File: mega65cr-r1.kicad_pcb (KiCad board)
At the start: 4 copper layers, 435 x 140.6 mm, 185 parts, among them J1 DB9_Male_MountingHoles, J10 Molex 46765-2301, J11 CON-SOCJ-2155, J12 Header for power lead to QMTE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, J13 Conn_01x04_Male, J14 Conn_02x17_Odd_Even, J15 696101000002 Fuse Holder 20mm, J16 Conn_01x04_Male, J17 C64_Tape_Port, J18 BA60BC0WT, J19 C64_User_Port, J2 DB9_Male_MountingHoles, J20 C64_Expansion_Port, J21 Audio Header, J22 DB15_Female_HighDensity_Mount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, J23 3.5mm_Stereo_Audio_Jack STX-3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, J24 Component A/V, J25 Joystick Ports Mezannine Lower, J26 Joystick Ports Mezannine Upper, J3 Wuerth_7499010121A, J4 QMTECH FPGA Module U4, J5 QMTECH FPGA Module U5, J6 SDF-60J for IEC 1541 serial p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, J7 QMTECH JTAG, J8 RTC, J9 1140084168 microSD Card Slot, P1 Full-side CD Card Slot, SW1 SW_Push_DPDT, SW2 SW_SPDT_with_shield, U1 74LS373, U10 74LS06N, U11 74LS06N, U12 DP83826, U13 74LVC374, U14 PTN3363BSMP, U15 LM2678T-5.0, U16 74LVC374, U17 74LVC374, U18 74LS374, U19 74LS374, U2 74LVC374, U20 74LS125, U21 74LS125, U22 74LS06N, U23 74LVC374, U24 74LS125, U25 74LS374, U26 74LS374, U27 74LS138, U28 74LS138, U29 74LS137, U3 74LVC374, U30 74LS137, U31 74LS04, U32 74LVC374, U33 74LVC374, U34 74LVC374, U35 74LS374, U36 74LS374, U37 74LS374, U38 74LVC374, U39 74LVC374, U4 74LS373, U40 74LS374, U41 74LS374, U5 74LS06N, U6 74LVC374, U7 74LVC374, U8 74LS374, U9 74LS373

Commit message: place some mounting holes and reset button #3
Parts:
- added H1: MountingHole_Pad, MountingHole:MountingHole_3.2mm_M3_DIN965_Pad, F.Cu at (35.0, 55.0)
- added H2: MountingHole_Pad, MountingHole:MountingHole_3.2mm_M3_DIN965_Pad, F.Cu at (62.0, 144.0)
- added H3: MountingHole_Pad, MountingHole:MountingHole_3.2mm_M3_DIN965_Pad, F.Cu at (331.8, 85.6)
- added H4: MountingHole_Pad, MountingHole:MountingHole_3.2mm_M3_DIN965_Pad, F.Cu at (338.9, 85.6)
- added H5: MountingHole_Pad, MountingHole:MountingHole_3.2mm_M3_DIN965_Pad, F.Cu at (331.8, 92.8)
- added H6: MountingHole_Pad, MountingHole:MountingHole_3.2mm_M3_DIN965_Pad, F.Cu at (324.6, 99.9)
- added H7: MountingHole_Pad, MountingHole:MountingHole_3.2mm_M3_DIN965_Pad, F.Cu at (324.6, 92.8)
- added H8: MountingHole_Pad, MountingHole:MountingHole_3.2mm_M3_DIN965_Pad, F.Cu at (317.5, 85.6)
- added H9: MountingHole_Pad, MountingHole:MountingHole_3.2mm_M3_DIN965_Pad, F.Cu at (317.5, 99.9)
- added J27: USB Blaster JTAG, Connector_PinHeader_2.54mm:PinHeader_2x05_P2.54mm_Vertical, F.Cu at (323.4, 113.4)
- added J28: UART, Connector_PinHeader_2.54mm:PinHeader_1x03_P2.54mm_Vertical, F.Cu at (316.2, 128.2)
- added J30: Keyboard JTAG header, Connector_PinHeader_2.54mm:PinHeader_2x05_P2.54mm_Vertical, F.Cu at (316.2, 113.4)
- added JP1: KBD JTAG EN, Connector_PinHeader_2.54mm:PinHeader_1x03_P2.54mm_Vertical, F.Cu at (330.6, 113.4)
- added U43: 74LVC374, Package_DIP:DIP-20_W7.62mm, F.Cu at (273.8, 84.1)
- added U44: 74LS374, Package_DIP:DIP-20_W7.62mm, F.Cu at (284.7, 84.1)
- J23: value 3.5mm_Stereo_Audio_Jack STX-3500-4N -> Audio Out
- JB1: value TE0790-03 -> TE0790-03 JTAG + UART
- SW1: value SW_Push_DPDT -> Reset Button
- moved SW1 43.5 mm to (48.0, 144.0), turned to 90 degrees
- moved J25 17.5 mm to (109.1, 135.1)
- moved J2 14.3 mm to (40.9, 115.5)
- moved J1 12.5 mm to (41.0, 84.0)
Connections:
- net /Cartridge Port/NMI_N renamed NMI_N
- net /FPGA Module/BANK12_N26 renamed KB_IO3
- net /FPGA Module/BANK12_P23 renamed KB_IO2
- net /FPGA Module/BANK12_R25 renamed KB_IO1
- net /Power Supply/VBAT renamed /Power Supply & Mounting Holes/VBAT
- net /VGA & Component AV/COMP_CHROMA renamed /VGA, C64 AV & C64 Keyboard/COMP_CHROMA
- net /VGA & Component AV/COMP_LUMA renamed /VGA, C64 AV & C64 Keyboard/COMP_LUMA
- net /VGA & Component AV/VGA_B renamed /VGA, C64 AV & C64 Keyboard/VGA_B
- net /VGA & Component AV/VGA_G renamed /VGA, C64 AV & C64 Keyboard/VGA_G
- net /VGA & Component AV/VGA_R renamed /VGA, C64 AV & C64 Keyboard/VGA_R
- net /VGA & Component AV/VGA_SCL renamed /VGA, C64 AV & C64 Keyboard/VGA_SCL
- net /VGA & Component AV/VGA_SDA renamed /VGA, C64 AV & C64 Keyboard/VGA_SDA
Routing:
- net /Power Supply & Mounting Holes/VBAT: track 74.1 -> 76.7 mm

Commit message: add and position mounting holes #3
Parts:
- added H10: MountingHole_Pad, MountingHole:MountingHole_3.2mm_M3_DIN965_Pad, F.Cu at (257.0, 50.0)
- added H11: MountingHole_Pad, MountingHole:MountingHole_3.2mm_M3_DIN965_Pad, F.Cu at (317.0, 50.0)
- added H12: MountingHole_Pad, MountingHole:MountingHole_3.2mm_M3_DIN965_Pad, F.Cu at (335.0, 40.0)
- added H13: MountingHole_Pad, MountingHole:MountingHole_3.2mm_M3_DIN965_Pad, F.Cu at (365.0, 40.0)
- added H14: MountingHole_Pad, MountingHole:MountingHole_3.2mm_M3_DIN965_Pad, F.Cu at (375.0, 40.0)
- added H15: MountingHole_Pad, MountingHole:MountingHole_3.2mm_M3_DIN965_Pad, F.Cu at (405.0, 40.0)
- added H16: MountingHole_Pad, MountingHole:MountingHole_3.2mm_M3_DIN965_Pad, F.Cu at (257.0, 110.0)
- added H17: MountingHole_Pad, MountingHole:MountingHole_3.2mm_M3_DIN965_Pad, F.Cu at (317.0, 110.0)
- moved H5 211.6 mm to (122.0, 64.9)
- moved H6 207.4 mm to (122.0, 144.0)
- moved H3 197.2 mm to (137.0, 55.0)
- moved H9 151.0 mm to (460.0, 50.0)
- moved H8 108.5 mm to (420.0, 50.0)
- moved H4 105.0 mm to (238.5, 55.0)
- moved H7 100.2 mm to (238.5, 144.0)
- moved J24 2.17 mm to (349.8, 37.9)

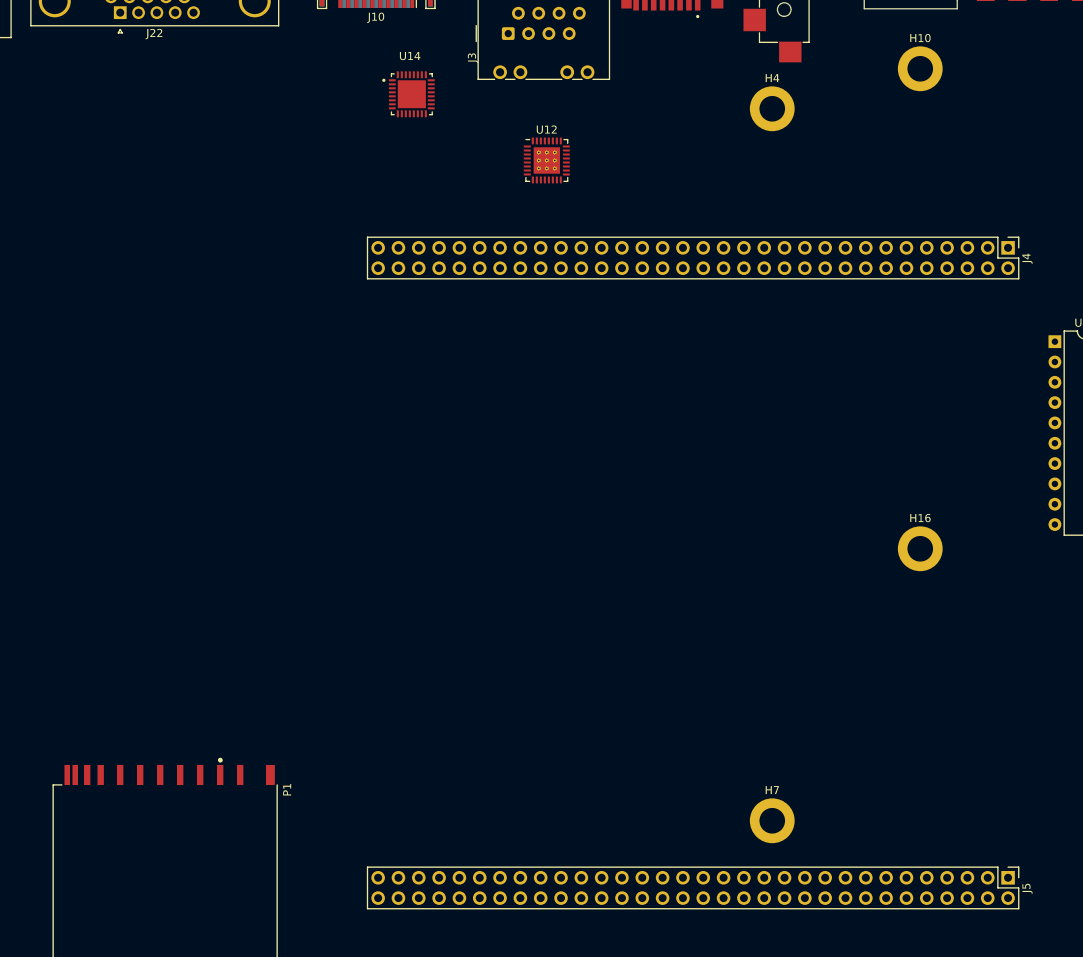
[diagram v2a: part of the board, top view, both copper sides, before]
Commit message: rearrange FPGA board connectors to detangle. Begin routing HDMI
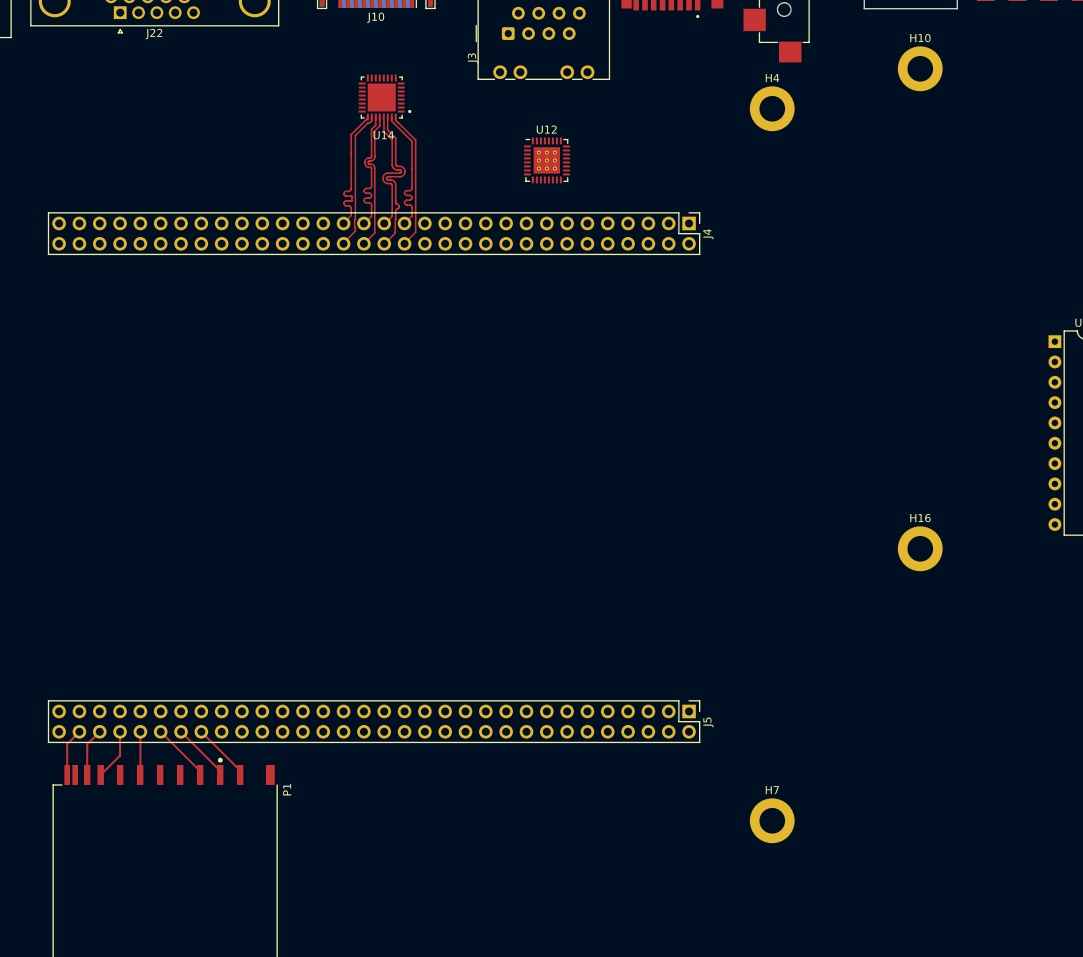
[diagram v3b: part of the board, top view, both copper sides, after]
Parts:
- moved J5 45.0 mm to (228.1, 130.3)
- moved J4 40.0 mm to (228.1, 69.3)
- moved U14 3.78 mm to (189.7, 53.6), turned to 180 degrees
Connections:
- J10 pad 1: Net-(J10-Pad1) -> /MEGA65 Peripherals, DVI, Eth, microSD/D2+
- J10 pad 10: Net-(J10-Pad10) -> /MEGA65 Peripherals, DVI, Eth, microSD/CK+
- J10 pad 12: Net-(J10-Pad12) -> /MEGA65 Peripherals, DVI, Eth, microSD/CK-
- J10 pad 3: Net-(J10-Pad3) -> /MEGA65 Peripherals, DVI, Eth, microSD/D2-
- J10 pad 4: Net-(J10-Pad4) -> /MEGA65 Peripherals, DVI, Eth, microSD/D1+
- J10 pad 6: Net-(J10-Pad6) -> /MEGA65 Peripherals, DVI, Eth, microSD/D1-
- J10 pad 7: Net-(J10-Pad7) -> /MEGA65 Peripherals, DVI, Eth, microSD/D0+
- J10 pad 9: Net-(J10-Pad9) -> /MEGA65 Peripherals, DVI, Eth, microSD/D0-
- J4 pad 10: COMP_CHROMA4 -> microSD_CLK
- J4 pad 11: MUX_A2 -> microSD_D2
- J4 pad 12: COMP_CHROMA3 -> microSD_CMD
- J4 pad 13: MUX_A3 -> ETH_TX_D0
- J4 pad 14: COMP_CHROMA2 -> ETH_RX_CLK
- J4 pad 15: MUX_DO0 -> ETH_TX_D1
- J4 pad 16: COMP_CHROMA1 -> ETH_RX_ER
- J4 pad 17: MUX_DO1 -> ETH_TX_EN
- J4 pad 18: COMP_CHROMA0 -> ETH_COL_DETECT
- J4 pad 19: MUX_DO2 -> ETH_TX_CLK
- J4 pad 20: SDCARD_D0 -> ETH_MDIO
- J4 pad 21: MUX_DO3 -> ETH_RX_D0
- J4 pad 22: SDCARD_D1 -> ETH_MDC
- J4 pad 23: MUX_DO4 -> ETH_RX_D1
- J4 pad 24: SDCARD_D2 -> ETH_CLKIN
- J4 pad 25: MUX_DO5 -> ETH_RX_DV
- J4 pad 26: SDCARD_D3 -> HDMI_HPD
- J4 pad 27: MUX_DO6 -> HDMI_SCL
- J4 pad 28: SDCARD_CMD -> HDMI_SDA
- J4 pad 29: MUX_DO7 -> HDMI_D2-
- J4 pad 30: SDCARD_CLK -> HDMI_D2+
- J4 pad 31: MUX_DI0 -> HDMI_D1-
- J4 pad 32: UART_RX -> HDMI_D1+
- J4 pad 33: MUX_DI1 -> HDMI_D0-
- J4 pad 34: UART_TX -> HDMI_D0+
- J4 pad 35: MUX_DI2 -> HDMI_CK-
- J4 pad 36: microSD_D0 -> HDMI_CK+
- J4 pad 37: MUX_DI3 -> VGA_R5
- J4 pad 38: microSD_D1 -> UART_RX
- J4 pad 39: MUX_DI4 -> VGA_R4
- J4 pad 40: microSD_D2 -> UART_TX
- J4 pad 41: MUX_DI5 -> VGA_R3
- J4 pad 42: microSD_D3 -> KB_IO1
- J4 pad 43: MUX_DI6 -> VGA_R2
- J4 pad 44: microSD_CLK -> VGA_B5
- J4 pad 45: MUX_DI7 -> VGA_R1
- J4 pad 46: microSD_CMD -> VGA_B4
- J4 pad 47: ETH_TX_D0 -> VGA_R0
- J4 pad 48: ETH_RX_CLK -> VGA_B3
- J4 pad 49: ETH_TX_D1 -> VGA_G5
- J4 pad 50: ETH_RX_ER -> VGA_B2
- J4 pad 51: ETH_TX_EN -> VGA_G4
- J4 pad 52: ETH_COL_DETECT -> VGA_B1
- J4 pad 53: ETH_TX_CLK -> VGA_G3
- J4 pad 54: ETH_MDIO -> VGA_B0
- J4 pad 55: ETH_RX_D0 -> VGA_G2
- J4 pad 56: ETH_MDC -> VGA_HSYNC
- J4 pad 57: ETH_RX_D1 -> VGA_G1
- J4 pad 58: ETH_CLKIN -> VGA_VSYNC
- J4 pad 59: ETH_RX_DV -> VGA_G0
- J4 pad 60: /FPGA Module/BANK16_D26 -> DOTCLOCK_O
- J4 pad 7: MUX_A0 -> microSD_D0
- J4 pad 8: COMP_CHROMA5 -> microSD_D3
- J4 pad 9: MUX_A1 -> microSD_D1
- J5 pad 10: HDMI_D1- -> COMP_CHROMA4
- J5 pad 11: HDMI_D0+ -> AUDIO_R3
- J5 pad 12: HDMI_D0- -> COMP_CHROMA3
- J5 pad 13: HDMI_CK+ -> AUDIO_R2
- J5 pad 14: HDMI_CK- -> COMP_CHROMA2
- J5 pad 15: HDMI_SCL -> AUDIO_R1
- J5 pad 16: AUDIO_L5 -> COMP_CHROMA1
- J5 pad 17: HDMI_SDA -> AUDIO_R0
- J5 pad 18: VGA_HSYNC -> COMP_CHROMA0
- J5 pad 19: HDMI_HPD -> AUDIO_L5
- J5 pad 20: VGA_VSYNC -> COMP_LUMA5
- J5 pad 21: AUDIO_R5 -> AUDIO_L4
- J5 pad 22: VGA_R5 -> COMP_LUMA4
- J5 pad 23: AUDIO_R4 -> AUDIO_L3
- J5 pad 24: VGA_R4 -> COMP_LUMA3
- J5 pad 25: AUDIO_R3 -> AUDIO_L2
- J5 pad 26: VGA_R3 -> COMP_LUMA2
- J5 pad 27: AUDIO_R2 -> AUDIO_L1
- J5 pad 28: VGA_R2 -> COMP_LUMA1
- J5 pad 29: AUDIO_R1 -> AUDIO_L0
- J5 pad 30: VGA_R1 -> COMP_LUMA0
- J5 pad 31: AUDIO_R0 -> MUX_DI0
- J5 pad 32: VGA_R0 -> MUX_DO0
- J5 pad 33: AUDIO_L4 -> MUX_DI1
- J5 pad 34: VGA_G5 -> MUX_DO1
- J5 pad 35: AUDIO_L3 -> MUX_DI2
- J5 pad 36: VGA_G4 -> MUX_DO2
- J5 pad 37: AUDIO_L2 -> MUX_DI3
- J5 pad 38: VGA_G3 -> MUX_DO3
- J5 pad 39: AUDIO_L1 -> MUX_DI4
- J5 pad 40: VGA_G2 -> MUX_DO4
- J5 pad 41: AUDIO_L0 -> MUX_DI5
- J5 pad 42: VGA_G1 -> MUX_DO5
- J5 pad 43: COMP_LUMA5 -> MUX_DI6
- J5 pad 44: VGA_G0 -> MUX_DO6
- J5 pad 45: COMP_LUMA4 -> MUX_DI7
- J5 pad 46: VGA_B5 -> MUX_DO7
- J5 pad 47: COMP_LUMA3 -> MUX_A0
- J5 pad 48: VGA_B4 -> /FPGA Module/BANK12_V24
- J5 pad 49: COMP_LUMA2 -> MUX_A1
- J5 pad 50: VGA_B3 -> SDCARD_D2
- J5 pad 51: COMP_LUMA1 -> MUX_A2
- J5 pad 52: VGA_B2 -> SDCARD_D3
- J5 pad 53: COMP_LUMA0 -> MUX_A3
- J5 pad 54: VGA_B1 -> SDCARD_CMD
- J5 pad 55: KB_IO1 -> /FPGA Module/BANK12_R25
- J5 pad 56: VGA_B0 -> SDCARD_CLK
- J5 pad 58: DOTCLOCK_O -> SDCARD_D0
- J5 pad 60: /FPGA Module/BANK12_M26 -> SDCARD_D1
- J5 pad 7: HDMI_D2+ -> AUDIO_R5
- J5 pad 8: HDMI_D2- -> COMP_CHROMA5
- J5 pad 9: HDMI_D1+ -> AUDIO_R4
- U14 pad 10: Net-(J10-Pad12) -> /MEGA65 Peripherals, DVI, Eth, microSD/D2-
- U14 pad 11: Net-(J10-Pad7) -> /MEGA65 Peripherals, DVI, Eth, microSD/D1+
- U14 pad 12: Net-(J10-Pad9) -> /MEGA65 Peripherals, DVI, Eth, microSD/D1-
- U14 pad 13: Net-(J10-Pad4) -> /MEGA65 Peripherals, DVI, Eth, microSD/D0+
- U14 pad 14: Net-(J10-Pad6) -> /MEGA65 Peripherals, DVI, Eth, microSD/D0-
- U14 pad 15: Net-(J10-Pad1) -> /MEGA65 Peripherals, DVI, Eth, microSD/CK+
- U14 pad 16: Net-(J10-Pad3) -> /MEGA65 Peripherals, DVI, Eth, microSD/CK-
- U14 pad 25: HDMI_D2- -> HDMI_CK-
- U14 pad 26: HDMI_D2+ -> HDMI_CK+
- U14 pad 27: HDMI_D1- -> HDMI_D0-
- U14 pad 28: HDMI_D1+ -> HDMI_D0+
- U14 pad 29: HDMI_D0- -> HDMI_D1-
- U14 pad 30: HDMI_D0+ -> HDMI_D1+
- U14 pad 31: HDMI_CK- -> HDMI_D2-
- U14 pad 32: HDMI_CK+ -> HDMI_D2+
- U14 pad 9: Net-(J10-Pad10) -> /MEGA65 Peripherals, DVI, Eth, microSD/D2+
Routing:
- net HDMI_D1+: track 0.00 -> 20.2 mm
- net HDMI_D0-: track 0.00 -> 17.8 mm
- net HDMI_D0+: track 0.00 -> 17.7 mm
- net HDMI_CK-: track 0.00 -> 17.5 mm
- net HDMI_D2+: track 0.00 -> 17.5 mm
- net HDMI_CK+: track 0.00 -> 17.4 mm
- net HDMI_D2-: track 0.00 -> 17.4 mm
- net HDMI_D1-: track 0.00 -> 17.3 mm
- net SDCARD_CMD: track 0.00 -> 7.44 mm
- net SDCARD_D3: track 0.00 -> 7.42 mm
- net SDCARD_D2: track 0.00 -> 7.41 mm
- net SDCARD_D0: track 0.00 -> 6.40 mm
- net SDCARD_D1: track 0.00 -> 6.05 mm
- net GND: track 3.03 -> 9.06 mm
- net SDCARD_CLK: track 0.00 -> 5.41 mm
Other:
- board text added: "J4"

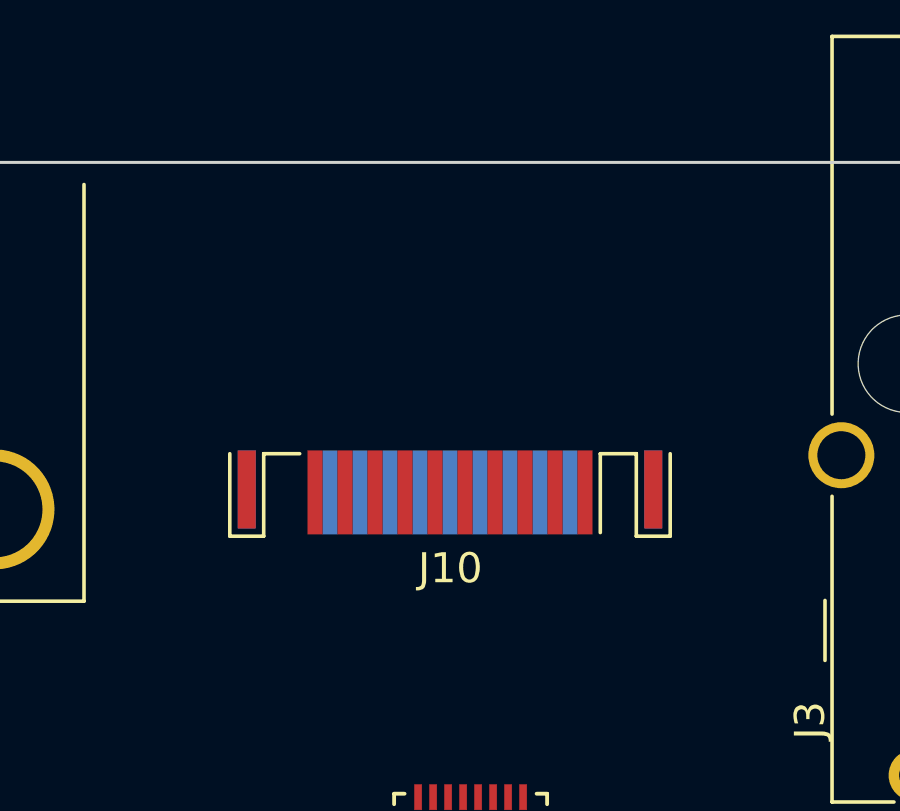
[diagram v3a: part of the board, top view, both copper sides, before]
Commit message: Replace HDMI connector #13
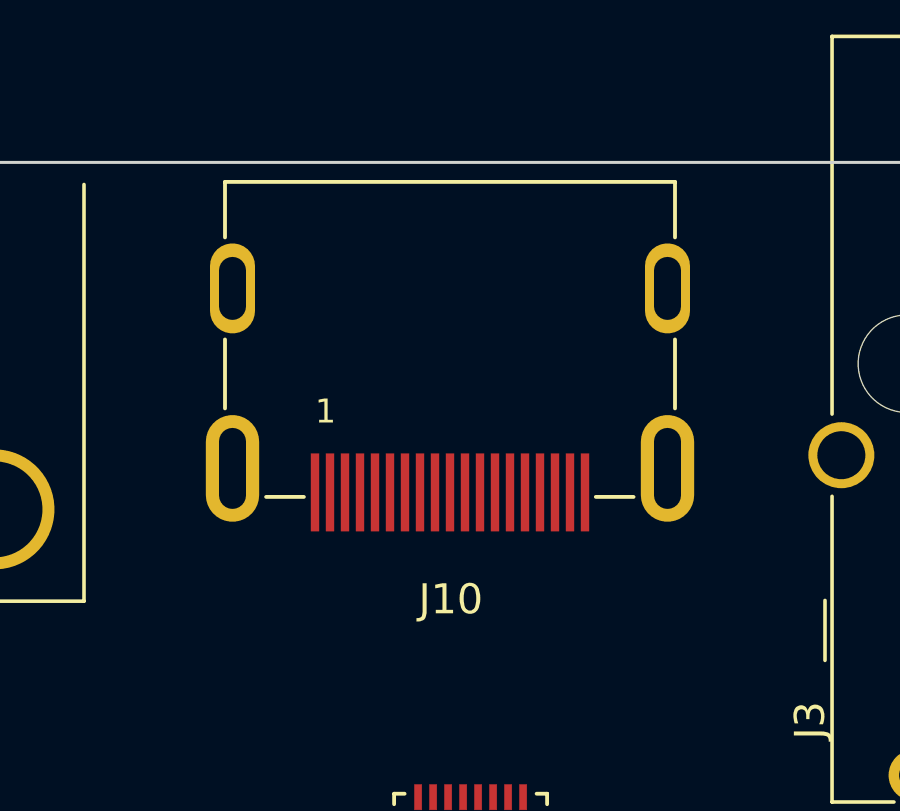
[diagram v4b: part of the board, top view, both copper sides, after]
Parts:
- J10: value Molex 46765-2301 -> 685119134923; footprint Connector_HDMI:HDMI_A_Contact_Technology_HDMI-19APL2_Horizontal -> snapeda:685119134923
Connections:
- net Net-(J10-Pad19) renamed /MEGA65 Peripherals, DVI, Eth, microSD/HPD_B
- J10 pad 11: Net-(J10-Pad11) -> GND
- J10 pad 17: Net-(J10-Pad11) -> GND
- J10 pad 18: unconnected-(J10-Pad18) -> +5V
- J10 pad 2: Net-(J10-Pad11) -> GND
- J10 pad 5: Net-(J10-Pad11) -> GND
- J10 pad 8: Net-(J10-Pad11) -> GND
- J4 pad 29: HDMI_D2- -> HDMI_CK-
- J4 pad 30: HDMI_D2+ -> HDMI_CK+
- J4 pad 31: HDMI_D1- -> HDMI_D0-
- J4 pad 32: HDMI_D1+ -> HDMI_D0+
- J4 pad 33: HDMI_D0- -> HDMI_D1-
- J4 pad 34: HDMI_D0+ -> HDMI_D1+
- J4 pad 35: HDMI_CK- -> HDMI_D2-
- J4 pad 36: HDMI_CK+ -> HDMI_D2+
- U14 pad 10: /MEGA65 Peripherals, DVI, Eth, microSD/D2- -> /MEGA65 Peripherals, DVI, Eth, microSD/CK-
- U14 pad 11: /MEGA65 Peripherals, DVI, Eth, microSD/D1+ -> /MEGA65 Peripherals, DVI, Eth, microSD/D0+
- U14 pad 12: /MEGA65 Peripherals, DVI, Eth, microSD/D1- -> /MEGA65 Peripherals, DVI, Eth, microSD/D0-
- U14 pad 13: /MEGA65 Peripherals, DVI, Eth, microSD/D0+ -> /MEGA65 Peripherals, DVI, Eth, microSD/D1+
- U14 pad 14: /MEGA65 Peripherals, DVI, Eth, microSD/D0- -> /MEGA65 Peripherals, DVI, Eth, microSD/D1-
- U14 pad 15: /MEGA65 Peripherals, DVI, Eth, microSD/CK+ -> /MEGA65 Peripherals, DVI, Eth, microSD/D2+
- U14 pad 16: /MEGA65 Peripherals, DVI, Eth, microSD/CK- -> /MEGA65 Peripherals, DVI, Eth, microSD/D2-
- U14 pad 25: HDMI_CK- -> HDMI_D2-
- U14 pad 26: HDMI_CK+ -> HDMI_D2+
- U14 pad 27: HDMI_D0- -> HDMI_D1-
- U14 pad 28: HDMI_D0+ -> HDMI_D1+
- U14 pad 29: HDMI_D1- -> HDMI_D0-
- U14 pad 30: HDMI_D1+ -> HDMI_D0+
- U14 pad 31: HDMI_D2- -> HDMI_CK-
- U14 pad 32: HDMI_D2+ -> HDMI_CK+
- U14 pad 9: /MEGA65 Peripherals, DVI, Eth, microSD/D2+ -> /MEGA65 Peripherals, DVI, Eth, microSD/CK+
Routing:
- net HDMI_D1+: track 20.2 -> 17.7 mm
- net HDMI_D0+: track 17.7 -> 20.2 mm
